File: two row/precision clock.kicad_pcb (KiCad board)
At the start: 2 copper layers, 155 x 53 mm, 48 parts, among them P1 USB_C_Plug_USB2.0, P2 USB_C_Plug_USB2.0, Q1 MMBT3906, Q2 MMBT3906

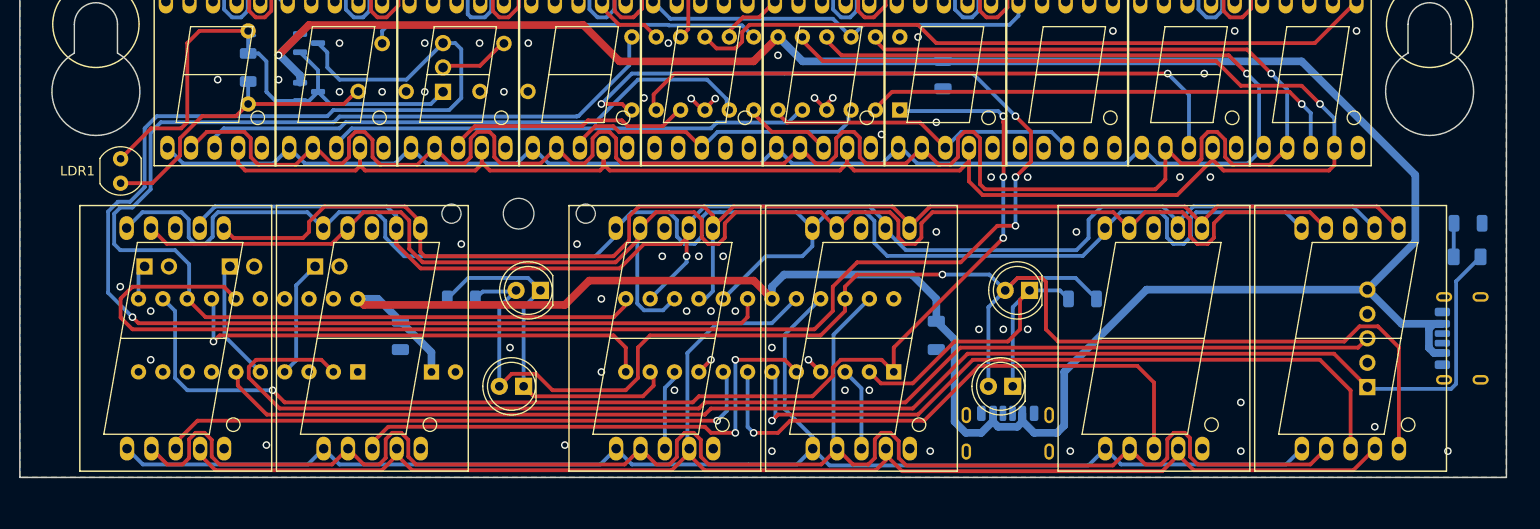
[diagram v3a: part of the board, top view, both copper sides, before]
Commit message: Fixed USB-C pinout and CC resistors
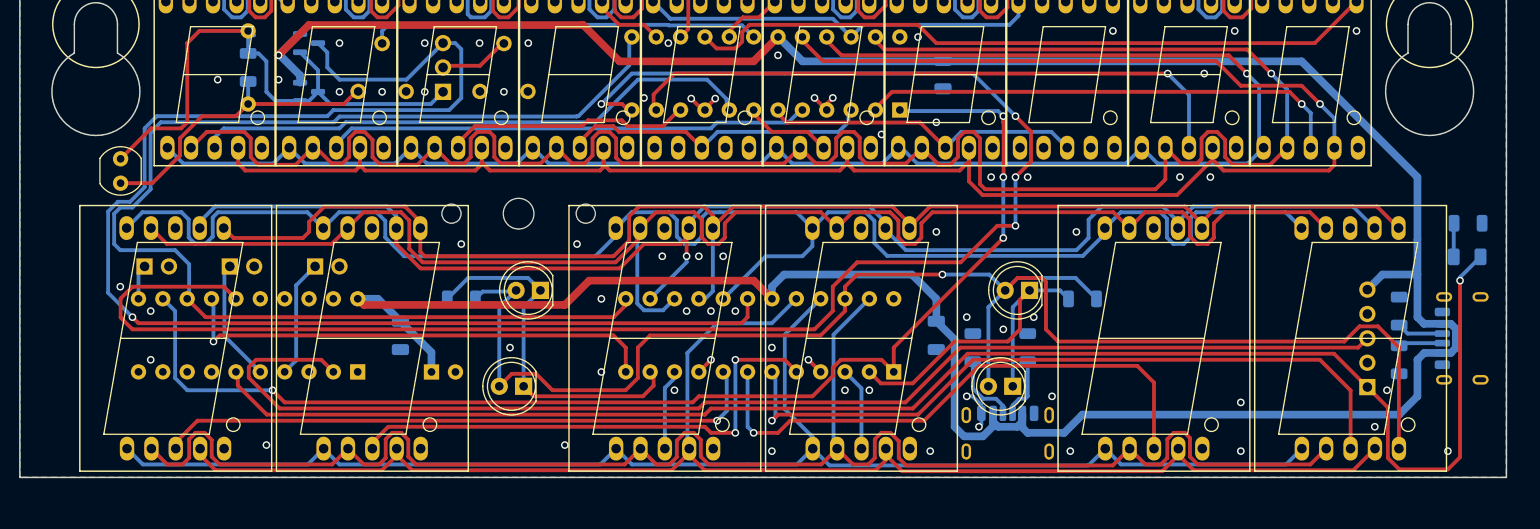
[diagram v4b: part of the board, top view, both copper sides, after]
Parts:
- added R1: 5.1k, Resistor_SMD:R_1206_3216Metric, B.Cu at (170.8, 102.2)
- added R2: 5.1k, Resistor_SMD:R_1206_3216Metric, B.Cu at (170.8, 97.2)
- added R4: 5.1k, Resistor_SMD:R_1206_3216Metric, B.Cu at (126.4, 101.0)
- added R5: 5.1k, Resistor_SMD:R_1206_3216Metric, B.Cu at (132.1, 101.0)
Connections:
- P1 pad A5: unconnected-(P1-CC-PadA5) -> Net-(P1-CC1)
- P1 pad B5: unconnected-(P1-VCONN-PadB5) -> Net-(P1-CC2)
- P2 pad A5: unconnected-(P2-CC-PadA5) -> Net-(P2-CC1)
- P2 pad B5: unconnected-(P2-VCONN-PadB5) -> Net-(P2-CC2)
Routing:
- net Net-(D_PPS1-A): track 148.1 -> 162.8 mm, vias 0 -> 1
- net Net-(P2-CC2): track 0.00 -> 7.47 mm
- net Net-(P2-CC1): track 0.00 -> 6.42 mm
- net +5V: track 313.0 -> 318.8 mm
- net Net-(P1-CC1): track 0.00 -> 4.87 mm
- net Net-(P1-CC2): track 0.00 -> 4.62 mm
- net GND: track 12.0 -> 16.3 mm, vias 62 -> 66

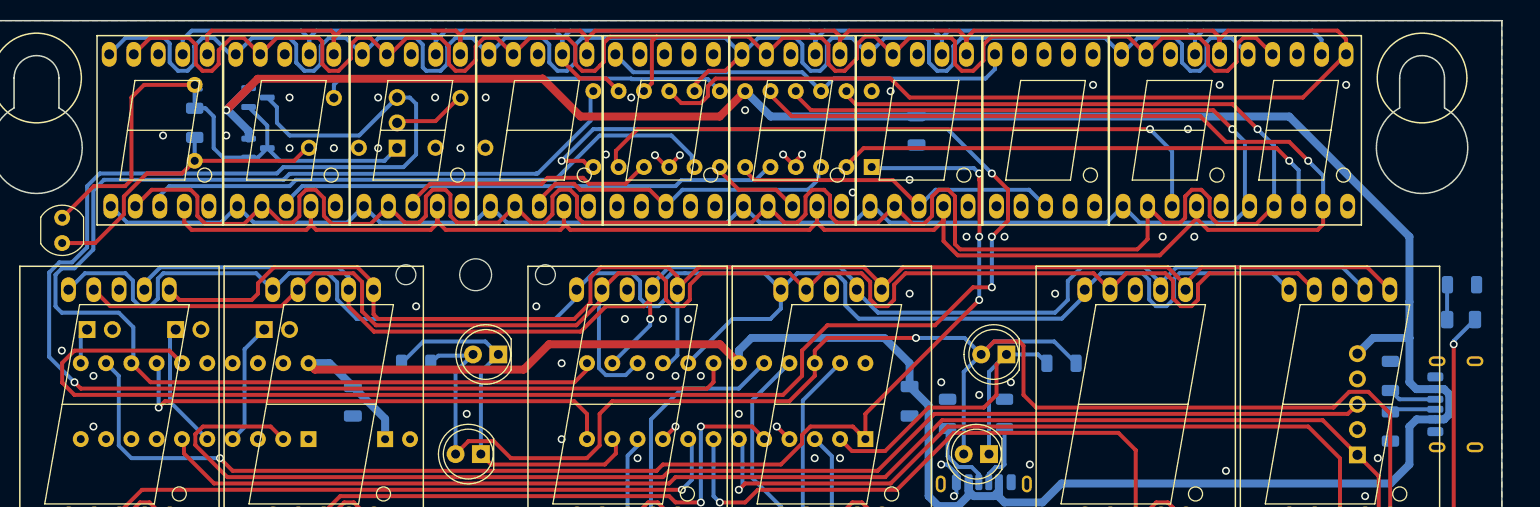
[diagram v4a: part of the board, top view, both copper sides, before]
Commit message: Fix reference designators
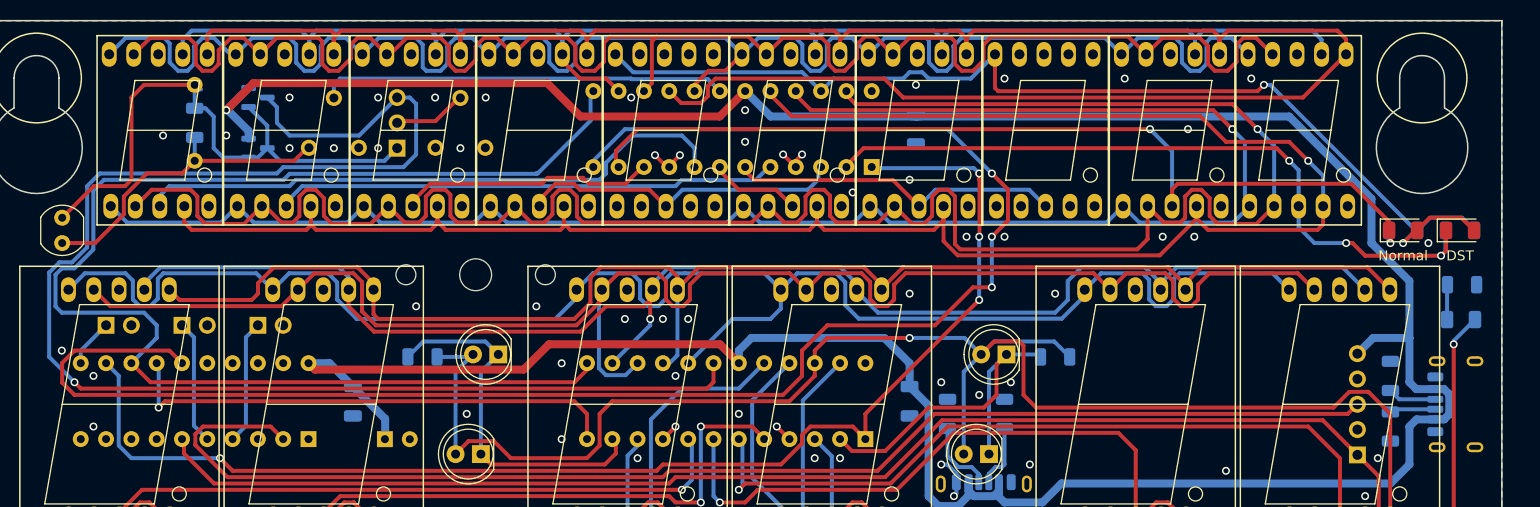
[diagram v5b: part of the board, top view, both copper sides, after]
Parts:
- removed JP5: UTC, Connector_PinHeader_2.54mm:PinHeader_1x02_P2.54mm_Vertical
- removed JP6: Perm_DST, Connector_PinHeader_2.54mm:PinHeader_1x02_P2.54mm_Vertical
- removed JP7: DST, Connector_PinHeader_2.54mm:PinHeader_1x02_P2.54mm_Vertical
- added D_BST1: DST, LED_SMD:LED_1206_3216Metric, F.Cu at (177.8, 82.5)
- added D_GMT1: Normal, LED_SMD:LED_1206_3216Metric, F.Cu at (172.1, 82.5)
- added JP1: Time_brt_mode, Connector_PinHeader_2.54mm:PinHeader_1x03_P2.54mm_Vertical, B.Cu at (71.1, 74.3)
- added JP2: UTC, Connector_PinHeader_2.54mm:PinHeader_1x02_P2.54mm_Vertical, B.Cu at (57.1, 92.1)
- added JP3: Perm_DST, Connector_PinHeader_2.54mm:PinHeader_1x02_P2.54mm_Vertical, B.Cu at (49.5, 92.1)
- added R7: 5.1k, Resistor_SMD:R_1206_3216Metric, B.Cu at (126.4, 101.0)
- added R8: 5.1k, Resistor_SMD:R_1206_3216Metric, B.Cu at (132.1, 101.0)
- C1: value C_Polarized_Small_US -> 0.1uF; footprint Capacitor_THT:CP_Radial_D5.0mm_P2.50mm -> Capacitor_SMD:C_1206_3216Metric
- C3: value 0.1uF -> C_Polarized_Small_US; footprint Capacitor_SMD:C_1206_3216Metric -> Capacitor_THT:CP_Radial_D5.0mm_P2.50mm
- JP4: value Time_brt_mode -> DST; footprint Connector_PinHeader_2.54mm:PinHeader_1x03_P2.54mm_Vertical -> Connector_PinHeader_2.54mm:PinHeader_1x02_P2.54mm_Vertical
- R1, R2, R4: value 5.1k -> 150
- R6: value 150 -> 5.1k
- moved R3 105.6 mm to (177.8, 82.5)
- moved R2 97.2 mm to (73.7, 95.2), turned to 0 degrees
- moved C3 61.7 mm to (69.9, 103.5), turned to 0 degrees
- moved C1 52.8 mm to (122.6, 99.7), turned to -90 degrees
- moved R5 38.8 mm to (170.8, 102.2), turned to -90 degrees
- moved JP4 34.2 mm to (41.9, 92.1), turned to -90 degrees
- moved R6 33.0 mm to (170.8, 97.2), turned to 90 degrees
- moved C2 27.3 mm to (123.2, 72.4)
- moved R1 19.7 mm to (172.1, 82.5), turned to 0 degrees
- moved R4 12.2 mm to (137.2, 95.2), turned to 0 degrees
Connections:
- DDay1 pad 3: Net-(UDateDrv1-DIG_0) -> Net-(D_BST1-K)
- DTenDay1 pad 3: Net-(UDateDrv1-DIG_1) -> Net-(D_GMT1-K)
- JP4 pad 1: Net-(JP4-A) -> /DST_EN*
- JP4 pad 2: Net-(JP4-C) -> GND
- LDR1 pad 1: Net-(JP4-A) -> Net-(JP1-A)
- Q1 pad 1: Net-(JP4-A) -> Net-(JP1-A)
- Q1 pad 3: Net-(JP4-A) -> Net-(JP1-A)
- Q2 pad 1: Net-(JP4-A) -> Net-(JP1-A)
- R1 pad 1: Net-(P1-CC2) -> Net-(D_GMT1-K)
- R1 pad 2: GND -> /dateDP
- R2 pad 1: Net-(P1-CC1) -> Net-(DColonHM1-K)
- R2 pad 2: GND -> /timeDP
- R3 pad 1: Net-(DColonHM1-K) -> Net-(D_BST1-K)
- R3 pad 2: /timeDP -> /dateDP
- R4 pad 1: Net-(P2-CC2) -> Net-(DColonMS1-K)
- R4 pad 2: GND -> /timeDP
- R5 pad 1: Net-(P2-CC1) -> Net-(P1-CC2)
- R6 pad 1: Net-(DColonMS1-K) -> Net-(P1-CC1)
- R6 pad 2: /timeDP -> GND
- R_Min_Bright1 pad 1: Net-(JP4-A) -> Net-(JP1-A)
- R_Min_Bright2 pad 1: Net-(JP4-A) -> Net-(JP1-A)
- R_Time_brt_adj1 pad 2: Net-(JP4-C) -> Net-(JP1-C)
- UDateDrv1 pad 11: Net-(UDateDrv1-DIG_1) -> Net-(D_GMT1-K)
- UDateDrv1 pad 2: Net-(UDateDrv1-DIG_0) -> Net-(D_BST1-K)
- U_CONTROL1 pad 4: Net-(JP5-A) -> /UTC*
- U_CONTROL1 pad 5: Net-(JP6-A) -> /PERM_DST*
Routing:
- net Net-(D_GMT1-K): track 0.00 -> 93.7 mm, vias 0 -> 2
- net Net-(D_BST1-K): track 0.00 -> 74.1 mm, vias 0 -> 3
- net /dateDP: track 42.0 -> 111.2 mm, vias 0 -> 2
- net Net-(UDateDrv1-DIG_1): track 64.9 -> 0.00 mm, vias 1 -> 0
- net Net-(JP4-A): track 57.2 -> 0.00 mm
- net Net-(JP1-A): track 0.00 -> 57.2 mm
- net Net-(UDateDrv1-DIG_0): track 51.0 -> 0.00 mm, vias 1 -> 0
- net Net-(JP6-A): track 12.8 -> 0.00 mm
- net /UTC*: track 0.00 -> 12.5 mm
- net /PERM_DST*: track 0.00 -> 12.5 mm
- net Net-(JP5-A): track 12.3 -> 0.00 mm
- net Net-(JP4-C): track 7.39 -> 0.00 mm
- net Net-(JP1-C): track 0.00 -> 7.39 mm
- net /LD_DATE: track 177.1 -> 171.4 mm, vias 4 -> 3
- net /SPI_CLK: track 129.8 -> 133.0 mm
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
